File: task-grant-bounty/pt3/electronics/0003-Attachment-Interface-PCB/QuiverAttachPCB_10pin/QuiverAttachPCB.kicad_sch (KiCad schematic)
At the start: 3 parts, among them J1 2077601281, J2 813-22-010-30-000101, J3 419-10-210-30-054000

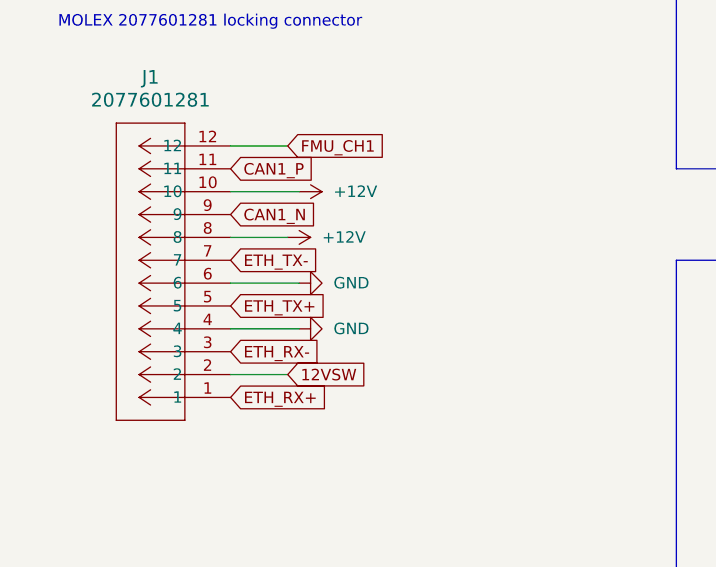
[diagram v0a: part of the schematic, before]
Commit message: Update PCB, docs based on feedbacl
- Update information note
- Change pin headers
- re-generate output files
- update images for documentation
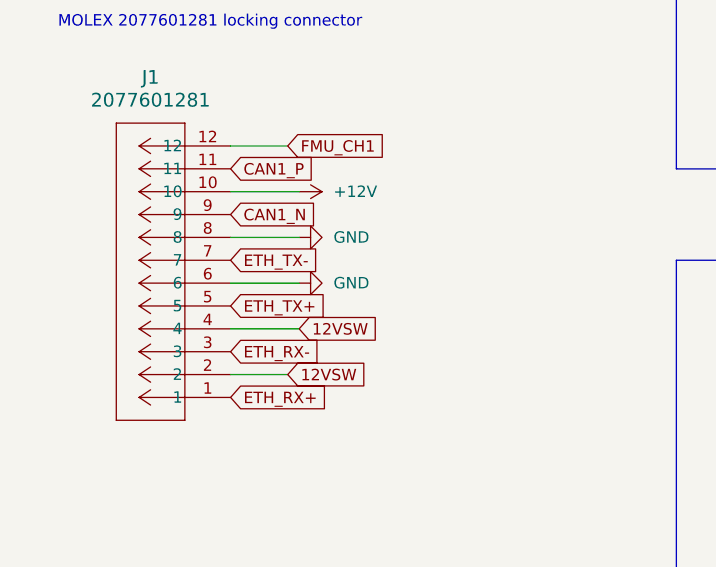
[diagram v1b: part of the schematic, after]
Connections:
- net +12V: no longer J1.8
- net 12VSW: now also J1.4
- net GND: now also J1.8; no longer J1.4
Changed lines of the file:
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@@
 	(title_block
 		(title "Project Quiver Attachment Interface PCB")
-		(date "2025-06-02")
+		(date "2025-06-08")
+		(rev "1.1")
 		(company "Arrow Air")
 	)
@@
 	(wire
 		(pts
-			(xy 78.74 104.14) (xy 85.09 104.14)
+			(xy 78.74 104.14) (xy 86.36 104.14)
 		)
 		(stroke
@@
 				)
 				(justify right)
+				(hide yes)
+			)
+		)
+	)
+	(global_label "12VSW"
+		(shape input)
+		(at 86.36 114.3 0)
+		(fields_autoplaced yes)
+		(effects
+			(font
+				(size 1.27 1.27)
+			)
+			(justify left)
+		)
+		(property "Intersheetrefs" "${INTERSHEET_REFS}"
+			(at 95.5137 114.3 0)
+			(effects
+				(font
+					(size 1.27 1.27)
+				)
+				(justify left)
 				(hide yes)
 			)
@@
 	(symbol
 		(lib_id "power:+12V")
-		(at 85.09 104.14 270)
-		(unit 1)
-		(exclude_from_sim no)
-		(in_bom yes)
-		(on_board yes)
-		(dnp no)
-		(fields_autoplaced yes)
-		(property "Reference" "#PWR02"
-			(at 81.28 104.14 0)
-			(effects
-				(font
-					(size 1.27 1.27)
-				)
-				(hide yes)
-			)
-		)
-		(property "Value" "+12V"
-			(at 88.9 104.1399 90)
-			(effects
-				(font
-					(size 1.27 1.27)
-				)
-				(justify left)
-			)
-		)
-		(property "Footprint" ""
-			(at 85.09 104.14 0)
-			(effects
-				(font
-					(size 1.27 1.27)
-				)
-				(hide yes)
-			)
-		)
-		(property "Datasheet" ""
-			(at 85.09 104.14 0)
-			(effects
-				(font
-					(size 1.27 1.27)
-				)
-				(hide yes)
-			)
-		)
-		(property "Description" "Power symbol creates a global label with name \"+12V\""
-			(at 85.09 104.14 0)
-			(effects
-				(font
-					(size 1.27 1.27)
-				)
-				(hide yes)
-			)
-		)
-		(pin "1"
-		)
-		(instances
-			(project "QuiverAttachPCB"
-				(path "/faf6ae05-859a-4da4-87ce-2d178afa08f0"
-					(reference "#PWR02")
-					(unit 1)
-				)
-			)
-		)
-	)
-	(symbol
-		(lib_id "power:+12V")
 		(at 86.36 99.06 270)
 		(unit 1)
@@
 	(symbol
 		(lib_id "power:GND")
-		(at 86.36 114.3 90)
+		(at 86.36 104.14 90)
 		(unit 1)
 		(exclude_from_sim no)
@@
 		(fields_autoplaced yes)
 		(property "Reference" "#PWR04"
-			(at 92.71 114.3 0)
+			(at 92.71 104.14 0)
 			(effects
 				(font
@@
 		)
 		(property "Value" "GND"
-			(at 90.17 114.2999 90)
+			(at 90.17 104.1399 90)
 			(effects
 				(font
@@
 		)
 		(property "Footprint" ""
-			(at 86.36 114.3 0)
+			(at 86.36 104.14 0)
 			(effects
 				(font
@@
 		)
 		(property "Datasheet" ""
-			(at 86.36 114.3 0)
+			(at 86.36 104.14 0)
 			(effects
 				(font
@@
 		)
 		(property "Description" "Power symbol creates a global label with name \"GND\" , ground"
-			(at 86.36 114.3 0)
-			(effects
-				(font
+			(at 86.36 104.14 0)
+			(effects
+				(font
